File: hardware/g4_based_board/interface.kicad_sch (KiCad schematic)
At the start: 39 parts, among them J8 USB_C_Receptacle_USB2.0, J9 Micro_SD_Card_Det1, Q1 NPN, Q2 NPN, SW3 DOWN, SW7 DOWN, SW8 DOWN, SW9 DOWN

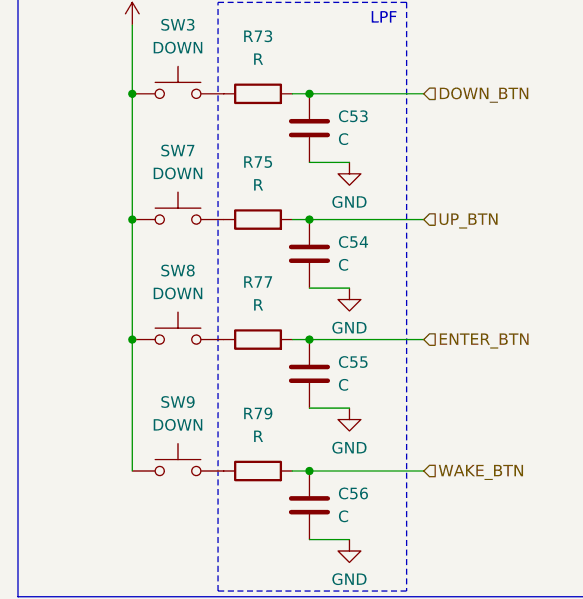
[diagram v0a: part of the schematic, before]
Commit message: added buttons
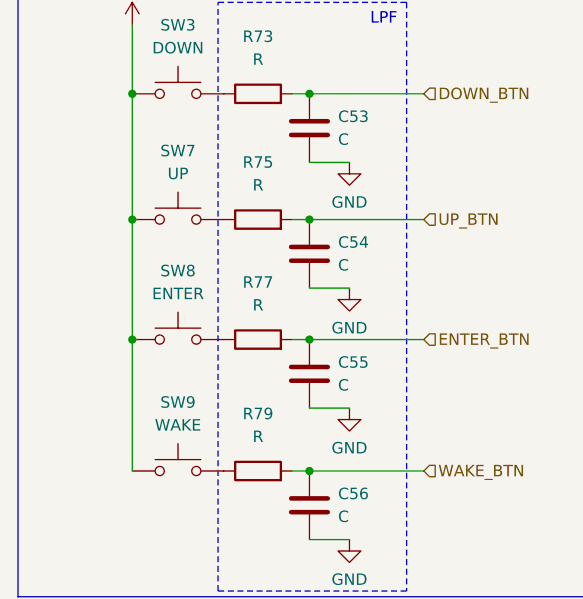
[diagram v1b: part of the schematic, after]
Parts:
- SW7: value DOWN -> UP
- SW8: value DOWN -> ENTER
- SW9: value DOWN -> WAKE
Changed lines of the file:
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@@
 			)
 		)
-		(property "Value" "DOWN"
+		(property "Value" "WAKE"
 			(at 33.02 126.365 0)
 			(effects
@@
 			)
 		)
-		(property "Value" "DOWN"
+		(property "Value" "UP"
 			(at 33.02 98.425 0)
 			(effects
@@
 			)
 		)
-		(property "Value" "DOWN"
+		(property "Value" "ENTER"
 			(at 33.02 111.76 0)
 			(effects

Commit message: rev-1
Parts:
- removed D6: SP0502BAHT, Package_TO_SOT_SMD:SOT-23, symbol Power_Protection:SP0502BAHT
- removed JP3, JP4, JP5, JP6, JP7: Jumper_2_Open, Jumper:SolderJumper-2_P1.3mm_Open_TrianglePad1.0x1.5mm, symbol Jumper:Jumper_2_Open
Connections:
- net MOSI: now also D4.3 (K); no longer D4.4 (K)
- net SCLK: now also D4.4 (K); no longer D4.6 (K)
- net SD_CONNECTED: now also D4.6 (K); no longer D4.3 (K)

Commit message: minor addtion and swd header added and usart removed
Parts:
- D5, D7: footprint LED_SMD:LED_0805_2012Metric -> LED_SMD:LED_0603_1608Metric
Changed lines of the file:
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@@
 			)
 		)
-		(property "Footprint" "LED_SMD:LED_0805_2012Metric"
+		(property "Footprint" "LED_SMD:LED_0603_1608Metric"
 			(at 228.6 27.305 0)
 			(effects
@@
 			)
 		)
-		(property "Footprint" "LED_SMD:LED_0805_2012Metric"
+		(property "Footprint" "LED_SMD:LED_0603_1608Metric"
 			(at 272.415 27.305 0)
 			(effects

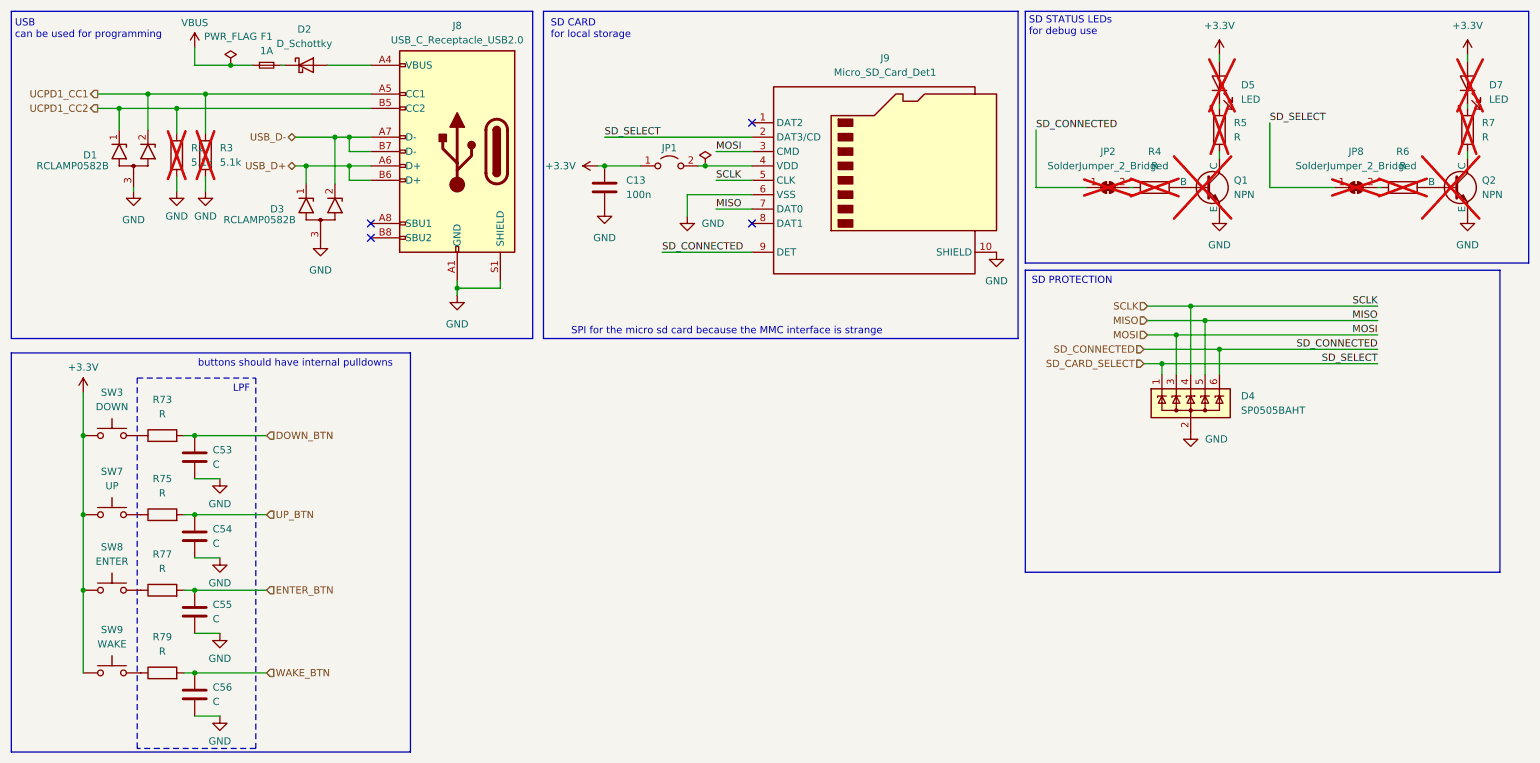
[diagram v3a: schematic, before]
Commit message: SD card protection now uses the CM1624, and removed buttons to be off board
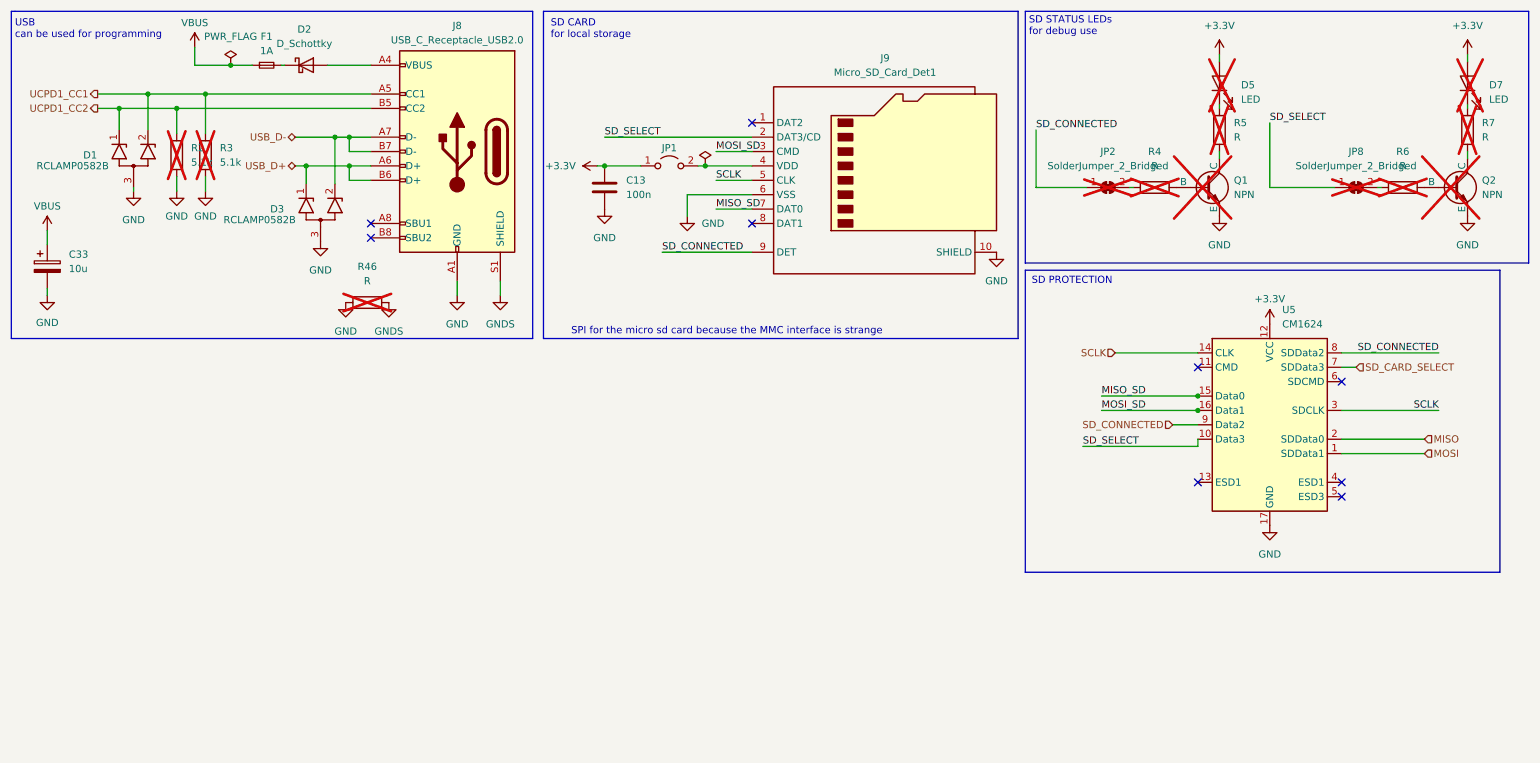
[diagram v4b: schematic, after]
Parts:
- removed C53, C54, C55, C56: C, Capacitor_SMD:C_0603_1608Metric_Pad1.08x0.95mm_HandSolder, symbol Device:C
- removed D4: SP0505BAHT, Package_TO_SOT_SMD:SOT-23-6, symbol Power_Protection:SP0505BAHT
- removed R73, R75, R77, R79: R, Resistor_SMD:R_0603_1608Metric_Pad0.98x0.95mm_HandSolder, symbol Device:R
- removed SW3: DOWN, Button_Switch_THT:SW_TH_Tactile_Omron_B3F-10xx, symbol Switch:SW_Push
- removed SW7: UP, Button_Switch_THT:SW_TH_Tactile_Omron_B3F-10xx, symbol Switch:SW_Push
- removed SW8: ENTER, Button_Switch_THT:SW_TH_Tactile_Omron_B3F-10xx, symbol Switch:SW_Push
- removed SW9: WAKE, Button_Switch_THT:SW_TH_Tactile_Omron_B3F-10xx, symbol Switch:SW_Push
- added C33: 10u, Capacitor_SMD:C_0603_1608Metric_Pad1.08x0.95mm_HandSolder, symbol Device:C_Polarized
- added R46: R, Resistor_SMD:R_0603_1608Metric_Pad0.98x0.95mm_HandSolder, symbol Device:R
- added U5: CM1624, Package_DFN_QFN:OnSemi_UDFN-16-1EP_1.35x3.3mm_P0.4mm_EP0.4x2.8mm, symbol Power_Protection:CM1624
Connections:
- net +3.3V: now also U5.12 (VCC)
- net GND: now also C33.2, R46.1, U5.17 (GND); no longer J8.S1 (SHIELD)
- net MISO: now also U5.2 (SDData0); no longer J9.7 (DAT0)
- net MOSI: now also U5.1 (SDData1); no longer J9.3 (CMD)
- net SCLK: now also U5.14 (CLK), U5.3 (SDCLK)
- net SD_CARD_SELECT: now also U5.7 (SDData3); no longer J9.2 (DAT3/CD), JP8.1 (A)
- net SD_CONNECTED: now also U5.8 (SDData2), U5.9 (Data2)
- net VBUS: now also C33.1
- new net GNDS: J8.S1 (SHIELD), R46.2
- new net MISO_SD: J9.7 (DAT0), U5.15 (Data0)
- new net MOSI_SD: J9.3 (CMD), U5.16 (Data1)
- new net SD_SELECT: J9.2 (DAT3/CD), JP8.1 (A), U5.10 (Data3)
- no-connect marks 4 -> 9
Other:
- note removed: "LPF"
- note removed: "buttons should have internal pulldowns"
